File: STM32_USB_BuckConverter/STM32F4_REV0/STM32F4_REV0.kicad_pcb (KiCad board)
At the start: 4 copper layers, 50 parts, among them J1 Screw_Terminal_01x02, J2 SWD, J3 Conn_01x04, J4 Conn_01x04, J5 USB_B_Micro, Q1 AO3401A, SW1 SW_SPDT, U1 MP2359DJ-LF-Z, U2 STM32F405RGT6, U3 USBLC6-2SC6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

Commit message: Updated PCB I2C pins, crystal oscillator setup.
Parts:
- moved C5 186.4 mm to (369.8, 149.0)
- moved C10 186.1 mm to (389.0, 149.0)
- moved C6 186.1 mm to (374.0, 149.0)
- moved C7 186.1 mm to (378.0, 149.0)
- moved C8 186.1 mm to (382.0, 149.0)
- moved C9 186.1 mm to (385.0, 149.0)
- moved C12 148.1 mm to (405.8, 121.7)
- moved R7 148.1 mm to (398.9, 125.7)
- moved C16 132.2 mm to (419.2, 142.5), turned to 180 degrees
- moved C15 129.4 mm to (419.2, 136.2)
- moved R8 128.6 mm to (423.0, 141.0), turned to 180 degrees
- moved J1 123.7 mm to (475.0, 201.0)
- moved C14 117.1 mm to (439.2, 137.2), turned to 270 degrees
- moved R11 109.0 mm to (431.5, 130.0), turned to 270 degrees
- moved C13 103.9 mm to (433.5, 148.2), turned to 180 degrees
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
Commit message: Finished layout of MCU.
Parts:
- moved C3 108.5 mm to (438.0, 160.2), turned to 0 degrees
- moved L1 102.3 mm to (436.5, 155.0), turned to 270 degrees
- moved D2 93.6 mm to (438.2, 149.8), turned to 0 degrees
- moved Q1 81.1 mm to (447.2, 145.2), turned to 270 degrees
- moved U1 80.8 mm to (442.2, 154.0), turned to 90 degrees
- moved J2 76.4 mm to (436.2, 124.2), turned to 90 degrees
- moved F1 76.2 mm to (443.6, 141.2), turned to 180 degrees
- moved C1 75.4 mm to (443.8, 149.8), turned to 0 degrees
- moved FB1 72.5 mm to (442.2, 145.5), turned to 270 degrees
- moved D1 69.1 mm to (448.0, 139.5), turned to 90 degrees
- moved J1 57.8 mm to (453.2, 147.5), turned to 90 degrees
- moved H3 54.4 mm to (472.5, 133.1)
- moved H1 54.4 mm to (482.7, 133.1)
- moved C5 54.3 mm to (421.5, 132.5), turned to 180 degrees
- moved C8 51.6 mm to (433.5, 146.2), turned to 0 degrees
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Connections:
- F1 pad 1: +12V -> Net-(D1-Pad1)
- FB1 pad 1: Net-(D1-Pad1) -> Net-(F1-Pad2)
- Q1 pad 3: Net-(F1-Pad2) -> +12V

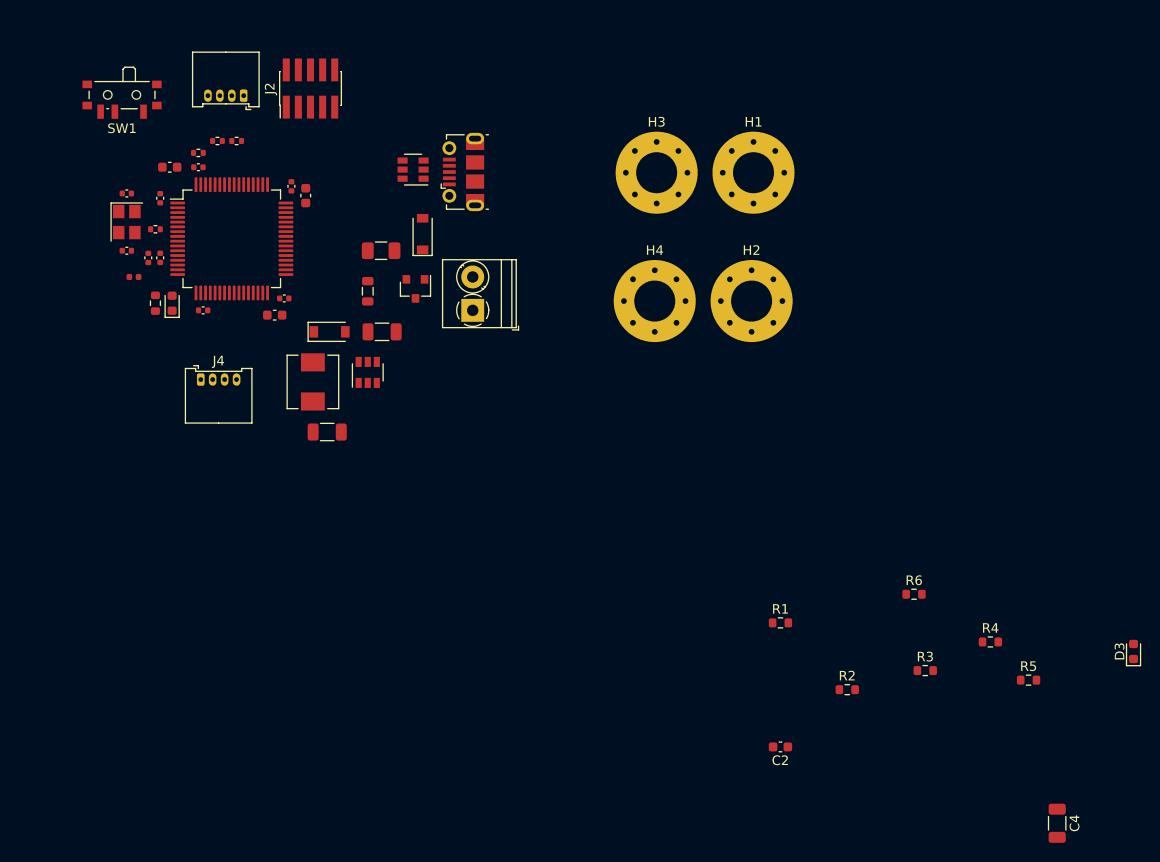
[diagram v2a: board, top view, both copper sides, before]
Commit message: Finished routing. Added vias for 3v3 and GND.
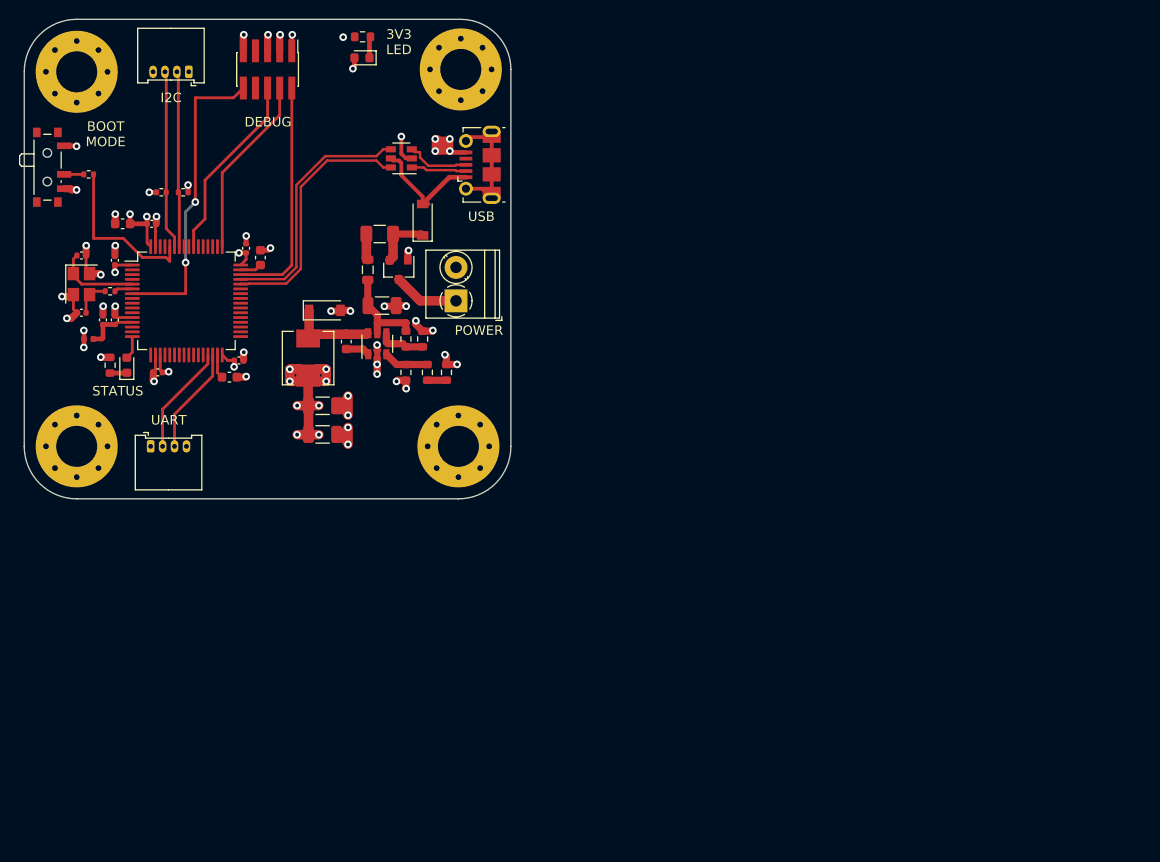
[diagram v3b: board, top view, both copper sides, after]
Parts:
- moved D3 102.0 mm to (441.6, 121.0), turned to 180 degrees
- moved C4 87.1 mm to (437.5, 160.5), turned to 0 degrees
- moved R6 82.2 mm to (441.7, 118.8)
- moved R5 69.0 mm to (450.5, 154.0), turned to 90 degrees
- moved H3 67.2 mm to (411.8, 161.8)
- moved R4 65.4 mm to (448.5, 154.0), turned to 270 degrees
- moved H4 65.2 mm to (411.8, 122.5)
- moved R3 62.8 mm to (446.2, 154.0), turned to 90 degrees
- moved C2 62.2 mm to (440.0, 150.8), turned to 90 degrees
- moved R2 57.7 mm to (448.0, 150.5), turned to 270 degrees
- moved R1 49.3 mm to (446.2, 150.5), turned to 90 degrees
- moved H2 34.3 mm to (451.8, 161.8)
- moved H1 32.5 mm to (452.0, 122.2)
- moved R7 11.7 mm to (413.0, 133.2)
- moved SW1 10.4 mm to (409.0, 132.5), turned to 270 degrees
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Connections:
- J3 pad 2: I2C1_SDA -> I2C1_SCL
- J3 pad 3: I2C1_SCL -> I2C1_SDA
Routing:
- net GND: track 0.00 -> 69.5 mm, vias 0 -> 41
- net +3V3: track 0.00 -> 51.1 mm, vias 0 -> 23
- net NRST: track 0.00 -> 32.0 mm, vias 0 -> 2
- net USB_D-: track 0.00 -> 26.5 mm
- net USB_D+: track 0.00 -> 26.5 mm
- net SWDIO: track 0.00 -> 24.3 mm
- net SWO: track 0.00 -> 19.8 mm
- net SWCLK: track 0.00 -> 19.1 mm
- net I2C1_SDA: track 0.00 -> 19.0 mm
- net I2C1_SCL: track 0.00 -> 18.4 mm
- net BOOT0: track 0.00 -> 17.2 mm
- net +5V: track 0.00 -> 13.0 mm
- net Net-(J5-Pad6): track 0.00 -> 12.4 mm
- net USART3_TX: track 0.00 -> 11.5 mm
- net USART3_RX: track 0.00 -> 11.2 mm
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- added copper zone on In2.Cu, net +3V3
- added copper zone on In1.Cu, net GND
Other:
- board outline added: 51 x 50.2 mm
- board text added: "3V3 LED"
- board text added: "BOOT MODE"
- board text added: "DEBUG"
- board text added: "I2C"
- board text added: "POWER"
- board text added: "STATUS"
- board text added: "UART"
- board text added: "USB"
